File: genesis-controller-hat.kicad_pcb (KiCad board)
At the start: 2 copper layers, 65 x 56 mm, 5 parts, among them J1 GPIO

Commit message: Place, wire, and route J2/J3 DB9 connectors on the PCB
Both DB9 sockets sit on the board's bottom edge (opposite J1, which runs
along the top), side by side, clearing the mounting holes and camera
slot. Built with the pcbnew Python API so net assignment goes through
KiCad's own net table by name. Routing uses a greedy two-layer assignment
with a per-net breakout waypoint, validated to cut DRC violations from
151 (naive single-layer straight-line routing) to 32 errors/5 warnings --
10 of those are pre-existing from Task 1's template, and the remaining
27 (mostly same-layer track crossings from this specific dense pinout)
are a disclosed, known follow-up requiring manual GUI routing cleanup
before fabrication, not a silent gap.

Co-Authored-By: Claude Sonnet 5 <noreply@anthropic.com>
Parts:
- added J2: DSUB-9_Socket_Vertical_P2.77x2.84mm_MountingHoles, DSUB-9_Socket_Vertical_P2.77x2.84mm_MountingHoles, F.Cu at (118.0, 84.0)
- added J3: DSUB-9_Socket_Vertical_P2.77x2.84mm_MountingHoles, DSUB-9_Socket_Vertical_P2.77x2.84mm_MountingHoles, F.Cu at (161.0, 84.0)
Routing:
- net GND: track 0.00 -> 79.9 mm
- net +3V3: track 0.00 -> 77.0 mm
- net /GPIO22: track 0.00 -> 52.6 mm
- net /GPIO23: track 0.00 -> 48.9 mm
- net /GPIO17: track 0.00 -> 48.4 mm
- net /GPIO6: track 0.00 -> 48.2 mm
- net /GPIO8/SPI0.CE0: track 0.00 -> 47.0 mm
- net /GPIO7/SPI0.CE1: track 0.00 -> 46.9 mm
- net /GPIO10/SPI0.MOSI: track 0.00 -> 45.6 mm
- net /GPIO5: track 0.00 -> 44.6 mm
- net /GPIO11/SPI0.SCLK: track 0.00 -> 44.2 mm
- net /GPIO9/SPI0.MISO: track 0.00 -> 42.5 mm
- net /GPIO12/PWM0: track 0.00 -> 40.8 mm
- net /GPIO4/GPCLK0: track 0.00 -> 38.1 mm
- net /GPIO16: track 0.00 -> 38.0 mm
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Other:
- board text added: "Player 1"
- board text added: "Player 2"

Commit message: Address final-review Minor findings: board rev silk, template cruft, parser hardening
Adds the board name/rev silkscreen the design spec called for but Task 6
missed; removes 7 leftover Dwgs.User annotations inherited from KiCad's
official RaspberryPi-HAT template (PoE/RJ45/USB/camera/display notes,
irrelevant to this DB9-only board); makes kicad_sexpr.py's parse_atom
raise on an unrecognized backslash-escape instead of silently dropping it
(inert today, but surfaces future corruption instead of hiding it);
reconciles two stale DRC-count references in the plan's Task 6 narrative
text to match the actually-delivered 32 errors/6 warnings.

Co-Authored-By: Claude Sonnet 5 <noreply@anthropic.com>
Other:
- board text added: "Genesis Controller HAT"
- board text added: "Rev A"
- board text removed: "CAMERA (OPTIONAL)"
- board text removed: "DISPLAY (OPTIONAL)"
- board text removed: "Extend PCB edge 0.5mm if using SMT header"
- board text removed: "PoE"
- board text removed: "RJ45"
- board text removed: "USB"
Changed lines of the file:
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@@
+		)
+	)
+	(gr_text "Genesis Controller HAT"
+		(at 140 58 0)
+		(layer "F.SilkS")
+		(effects
+			(font
+				(size 1.5 1.5)
+			)
+		)
+	)
+	(gr_text "Rev A"
+		(at 140 61 0)
+		(layer "F.SilkS")
+		(effects
+			(font
+				(size 1.5 1.5)
+			)
 		)
 	)
@@
 			(font
 				(size 1.5 1.5)
-			)
-		)
-	)
-	(gr_text "Extend PCB edge 0.5mm if using SMT header"
-		(at 103 42.5 0)
-		(layer "Dwgs.User")
-		(effects
-			(font
-				(size 1 1)
-				(thickness 0.15)
-			)
-			(justify left)
-		)
-	)
-	(gr_text "PoE"
-		(at 161.5 53.64 0)
-		(layer "Dwgs.User")
-		(effects
-			(font
-				(size 1 1)
-				(thickness 0.15)
-			)
-		)
-	)
-	(gr_text "DISPLAY (OPTIONAL)"
-		(at 102.5 72 90)
-		(layer "Dwgs.User")
-		(effects
-			(font
-				(size 1 1)
-				(thickness 0.15)
-			)
-		)
-	)
-	(gr_text "CAMERA (OPTIONAL)"
-		(at 145 88.5 90)
-		(layer "Dwgs.User")
-		(effects
-			(font
-				(size 1 1)
-				(thickness 0.15)
-			)
-		)
-	)
-	(gr_text "RJ45"
-		(at 176.2 89.84 0)
-		(layer "Dwgs.User")
-		(effects
-			(font
-				(size 2 2)
-				(thickness 0.15)
-			)
-		)
-	)
-	(gr_text "USB"
-		(at 177.724 71.552 0)
-		(layer "Dwgs.User")
-		(effects
-			(font
-				(size 2 2)
-				(thickness 0.15)
-			)
-		)
-	)
-	(gr_text "USB"
-		(at 178.232 52.248 0)
-		(layer "Dwgs.User")
-		(effects
-			(font
-				(size 2 2)
-				(thickness 0.15)
 			)
 		)
@@
 	)
 	(group ""
-		(members "1811fd1a-b55e-4d16-931d-f9ec6a9e16f7" "79c07597-5ab9-4d26-b4b3-a70ae9dcd11d"
-			"81e492f6-268f-4ce2-bb45-32834e67e85b" "b6c3db4f-e418-4da3-aef6-5010435bcf13"
-			"d4c39290-1388-499e-abdc-d2c7dce5190a"
-		)
-	)
+		(members "79c07597-5ab9-4d26-b4b3-a70ae9dcd11d" "81e492f6-268f-4ce2-bb45-32834e67e85b"
+			"b6c3db4f-e418-4da3-aef6-5010435bcf13" "d4c39290-1388-499e-abdc-d2c7dce5190a"
+		)
+	)

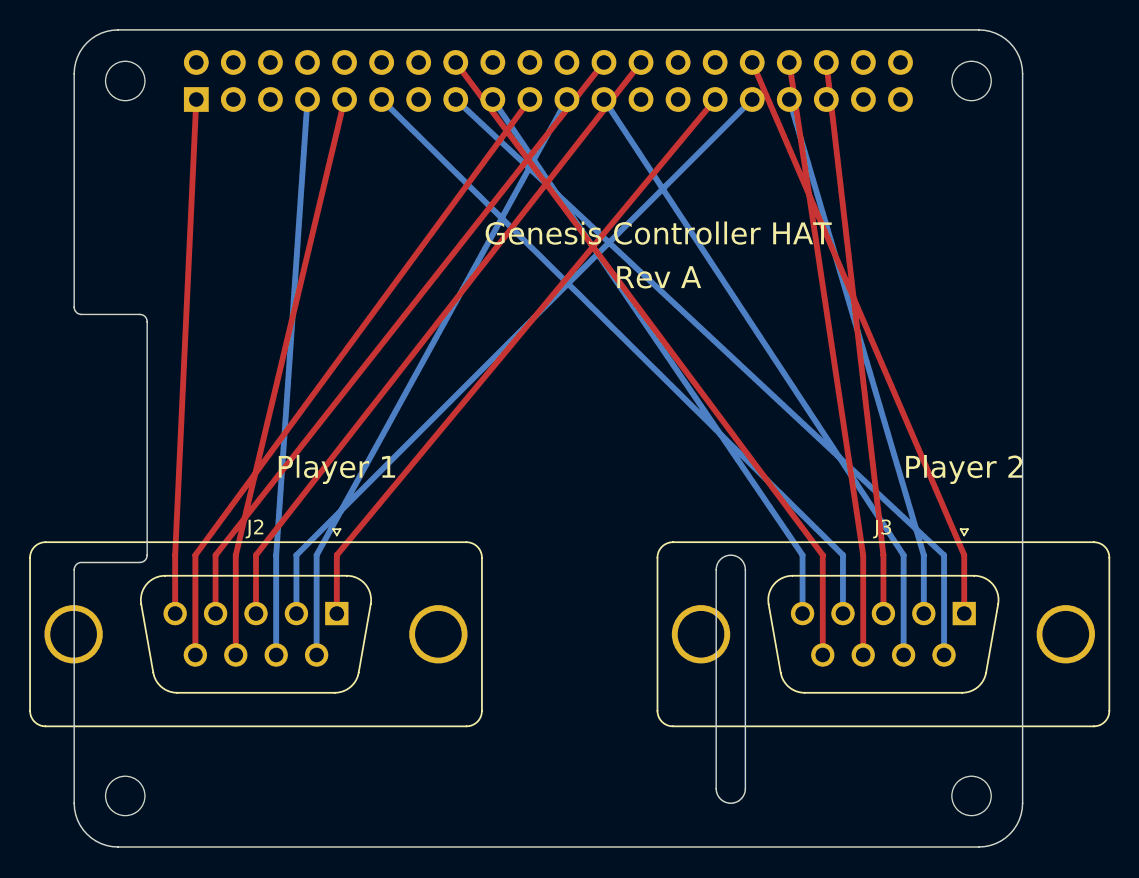
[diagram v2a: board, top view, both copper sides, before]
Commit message: Add GND ground pour on B.Cu; add kicad-happy design review
Adds a solid GND copper pour on B.Cu (fewer signal traces there than
F.Cu, and J1 already sits on that layer), using direct pad connections
rather than thermal-relief spokes -- simpler and more robust for a small
2-layer hobbyist board, and it avoids a min-spoke-count DRC rule these
particular THT pads couldn't satisfy with default thermal relief.
Removes a leftover unfilled "PoE" keepout zone inherited from KiCad's
official RaspberryPi-HAT template. Verified: unconnected_items dropped
9->2 (the pour ties together most of J1's previously-disconnected GND
pins), ERC unaffected (still 0/0), visually confirmed via render.

Also adds docs/reviews/2026-07-22-kicad-happy-review.md, the design
review that recommended this change (run via the newly-installed
kicad-happy plugin), and gitignores its regenerable analysis/ cache dir.

Co-Authored-By: Claude Sonnet 5 <noreply@anthropic.com>
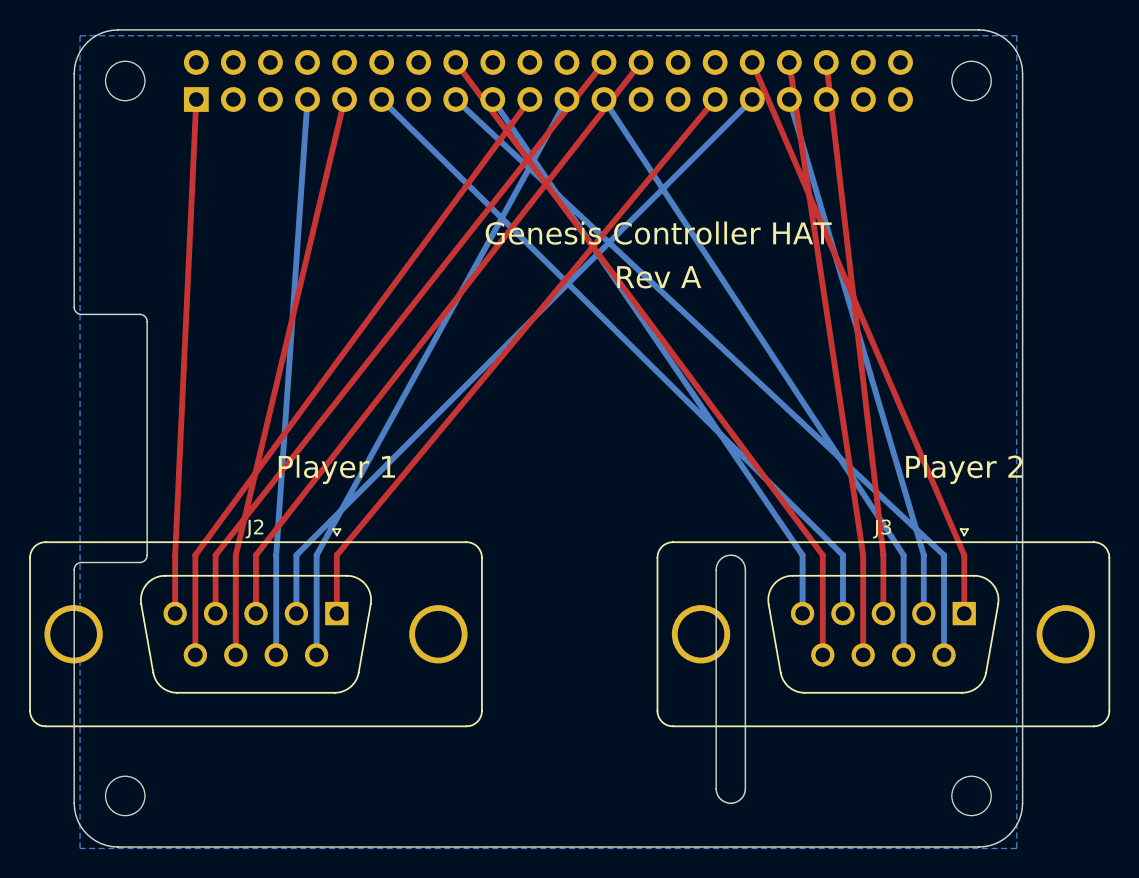
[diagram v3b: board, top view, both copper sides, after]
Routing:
- added copper zone on B.Cu, net GND
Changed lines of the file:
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@@
 	)
 	(zone
-		(net 0)
-		(net_name "")
+		(net 1)
+		(net_name "GND")
 		(layer "B.Cu")
-		(name "PoE")
-		(hatch full 0.508)
-		(connect_pads
+		(name "GND_POUR")
+		(hatch edge 0.5)
+		(connect_pads yes
 			(clearance 0)
 		)
-		(min_thickness 0.254)
+		(min_thickness 0.25)
 		(filled_areas_thickness no)
-		(keepout
-			(tracks allowed)
-			(vias allowed)
-			(pads allowed)
-			(copperpour allowed)
-			(footprints not_allowed)
-		)
-		(placement
-			(enabled no)
-			(sheetname "")
-		)
-		(fill
-			(thermal_gap 0.508)
-			(thermal_bridge_width 0.508)
+		(fill yes
+			(thermal_gap 0.5)
+			(thermal_bridge_width 0.5)
 		)
 		(polygon
 			(pts
-				(xy 164 56.14) (xy 159 56.14) (xy 159 51.14) (xy 164 51.14)
+				(xy 100.4 44.4) (xy 164.6 44.4) (xy 164.6 100.1) (xy 100.4 100.1)
 			)
 		)

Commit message: Reassign GPIO pin map to eliminate PCB routing crossings
Rewires J2/J3 to the new pin assignment (Port 1 select=22 data=10,23,27,17,24,4;
Port 2 select=12 data=26,13,6,5,16,7) that groups each port's signals onto
physically adjacent GPIO header columns nearest that port's connector. This
lets the board route with zero same-layer trace crossings and zero
hole-clearance violations (was 14 tracks_crossing + 4 hole_clearance),
reducing total DRC violations from 30 errors/6 warnings to 16/6. ERC remains
0/0, and the schematic wiring matches the firmware repo's updated
sega_board.h exactly (verified via scripts/check_pinmap.py).

See docs/reviews/2026-07-22-pinmap-reassignment.md for the full root-cause
analysis and before/after DRC breakdown.

Co-Authored-By: Claude Sonnet 5 <noreply@anthropic.com>
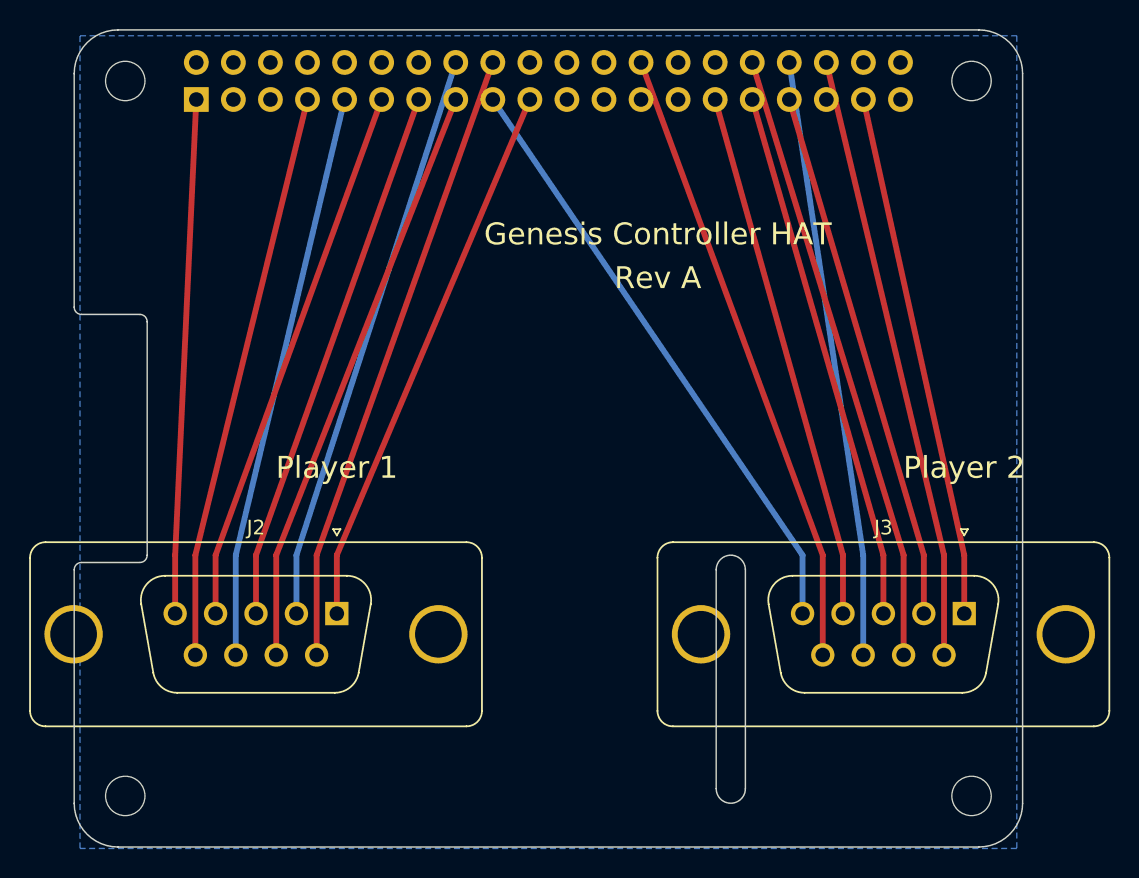
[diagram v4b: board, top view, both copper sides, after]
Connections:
- J2 pad 1: /GPIO5 -> /GPIO10/SPI0.MOSI
- J2 pad 2: /GPIO6 -> /GPIO23
- J2 pad 3: /GPIO7/SPI0.CE1 -> /GPIO27
- J2 pad 4: /GPIO8/SPI0.CE0 -> /GPIO17
- J2 pad 6: /GPIO9/SPI0.MISO -> /GPIO24
- J2 pad 7: /GPIO4/GPCLK0 -> /GPIO22
- J2 pad 9: /GPIO10/SPI0.MOSI -> /GPIO4/GPCLK0
- J3 pad 1: /GPIO12/PWM0 -> /GPIO26
- J3 pad 3: /GPIO16 -> /GPIO6
- J3 pad 4: /GPIO17 -> /GPIO5
- J3 pad 6: /GPIO22 -> /GPIO16
- J3 pad 7: /GPIO11/SPI0.SCLK -> /GPIO12/PWM0
- J3 pad 9: /GPIO23 -> /GPIO7/SPI0.CE1
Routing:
- net /GPIO8/SPI0.CE0: track 47.0 -> 0.00 mm
- net /GPIO11/SPI0.SCLK: track 44.2 -> 0.00 mm
- net /GPIO24: track 0.00 -> 42.7 mm
- net /GPIO9/SPI0.MISO: track 42.5 -> 0.00 mm
- net /GPIO27: track 0.00 -> 37.2 mm
- net /GPIO26: track 0.00 -> 36.0 mm
- net /GPIO22: track 52.6 -> 40.4 mm
- net /GPIO6: track 48.2 -> 36.5 mm
- net /GPIO17: track 48.4 -> 37.2 mm
- net /GPIO23: track 48.9 -> 39.5 mm
- net /GPIO5: track 44.6 -> 36.4 mm
- net /GPIO10/SPI0.MOSI: track 45.6 -> 37.9 mm
- net /GPIO7/SPI0.CE1: track 46.9 -> 42.8 mm
- net /GPIO16: track 38.0 -> 41.6 mm
- net /GPIO12/PWM0: track 40.8 -> 42.2 mm
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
